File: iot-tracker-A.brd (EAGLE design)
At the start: 21.6 x 19.6 mm, 27 parts, among them IC1 PCF85263ATL_AX, U1 ESP-WROOM-02, U2 TPL5111DDCR, U3 TPS61021ADSGR, Y1 FC-135_32.7680KA-AG3

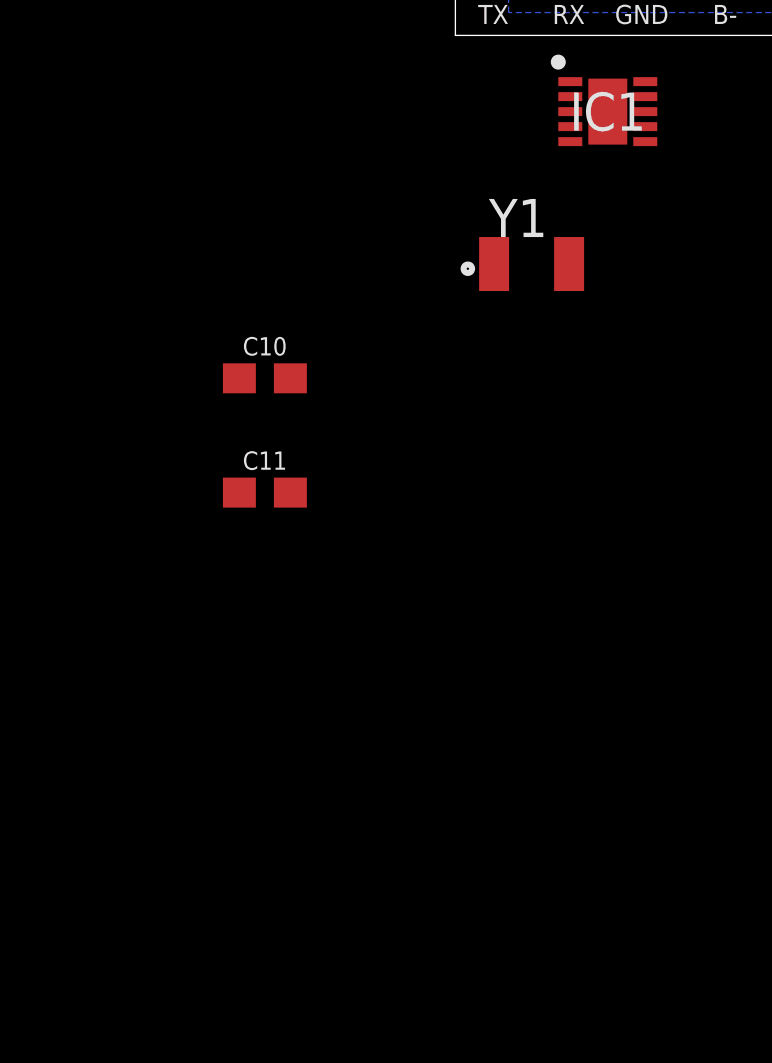
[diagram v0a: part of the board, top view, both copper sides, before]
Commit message: Changed crystal device and added the PNP for DRVN
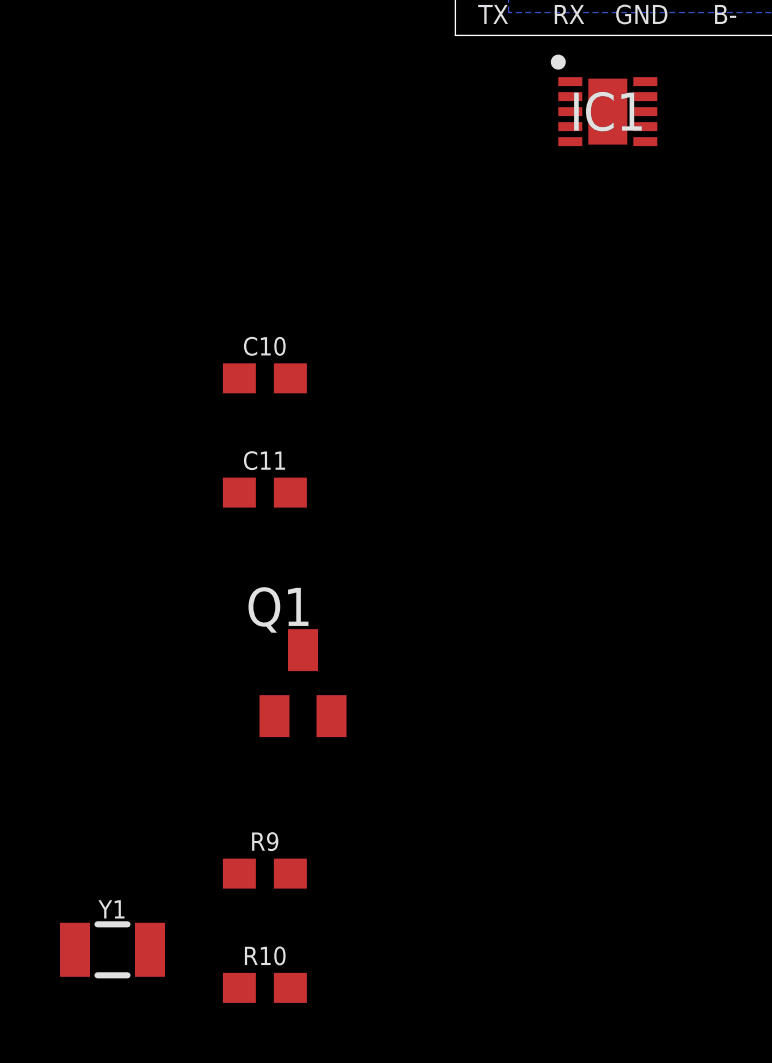
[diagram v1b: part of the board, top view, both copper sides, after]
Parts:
- added Q1: MMBT3906, transistor-pnp:SOT23-BEC
- added R10, R9: 100k, SparkFun-Resistors:0603
- Y1: value FC-135_32.7680KA-AG3 -> 32.768kHz; device IOT-Tracker-A:FC-135_1 -> SparkFun-Clocks:CRYSTAL-SMD-3.2X1.5MM
- moved Y1 26.8 mm to (-11.4, -30.5)
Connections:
- removed net OSCI: IC1.1, Y1.1
- new net N$1: IC1.9, R9.1
- new net N$2: Q1.B, R9.2
- new net N$3: IC1.1, Y1.P$2
- net DRVN: now also Q1.C, R10.2
- net GND: now also R10.1
- net OSCO: now also Y1.P$1; no longer Y1.2
- net V_BATT: now also Q1.E
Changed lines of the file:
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@@
 <attribute name="VALUE" x="5.08" y="-2.54" size="1.27" layer="27" align="center"/>
-</element>
-<element name="Y1" library="IOT-Tracker-A" package="FC-135_1" value="FC-135_32.7680KA-AG3" x="2.54" y="-7.62" smashed="yes">
-<attribute name="DESCRIPTION" value="Crystals 32.768KHz 20ppm 7.0pF -40C +85C" x="2.54" y="-7.62" size="1.778" layer="27" display="off"/>
-<attribute name="HEIGHT" value="mm" x="2.54" y="-7.62" size="1.778" layer="27" display="off"/>
-<attribute name="MANUFACTURER_NAME" value="Epson Timing" x="2.54" y="-7.62" size="1.778" layer="27" display="off"/>
-<attribute name="MANUFACTURER_PART_NUMBER" value="FC-135 32.7680KA-AG3" x="2.54" y="-7.62" size="1.778" layer="27" display="off"/>
-<attribute name="MOUSER_PART_NUMBER" value="732-FC135-32.76KAAG3" x="2.54" y="-7.62" size="1.778" layer="27" display="off"/>
-<attribute name="MOUSER_PRICE-STOCK" value="https://www.mouser.com/Search/Refine.aspx?Keyword=732-FC135-32.76KAAG3" x="2.54" y="-7.62" size="1.778" layer="27" display="off"/>
-<attribute name="NAME" x="2.09671875" y="-6.086340625" size="1.27" layer="25" align="center"/>
-<attribute name="VALUE" x="2.09671875" y="-6.086340625" size="1.27" layer="27" align="center"/>
 </element>
 <element name="C10" library="SparkFun-Capacitors" package="0603" value="0.1uF" x="-6.35" y="-11.43" smashed="yes">
@@
 <attribute name="PROD_ID" value="CAP-00810" x="-6.35" y="-15.24" size="1.778" layer="27" display="off"/>
 <attribute name="VALUE" x="-6.35" y="-16.002" size="0.6096" layer="27" font="vector" ratio="20" align="top-center"/>
+</element>
+<element name="Q1" library="transistor-pnp" library_urn="urn:adsk.eagle:library:399" package="SOT23-BEC" package3d_urn="urn:adsk.eagle:package:28748/2" value="MMBT3906" x="-5.08" y="-21.59" smashed="yes">
+<attribute name="NAME" x="-6.985" y="-19.685" size="1.27" layer="25"/>
+<attribute name="VALUE" x="-6.985" y="-24.765" size="1.27" layer="27"/>
+</element>
+<element name="R9" library="SparkFun-Resistors" package="0603" value="100k" x="-6.35" y="-27.94" smashed="yes">
+<attribute name="NAME" x="-6.35" y="-27.178" size="0.6096" layer="25" font="vector" ratio="20" align="bottom-center"/>
+<attribute name="PROD_ID" value="RES-07828" x="-6.35" y="-27.94" size="1.778" layer="27" display="off"/>
+<attribute name="VALUE" x="-6.35" y="-28.702" size="0.6096" layer="27" font="vector" ratio="20" align="top-center"/>
+</element>
+<element name="R10" library="SparkFun-Resistors" package="0603" value="100k" x="-6.35" y="-31.75" smashed="yes">
+<attribute name="NAME" x="-6.35" y="-30.988" size="0.6096" layer="25" font="vector" ratio="20" align="bottom-center"/>
+<attribute name="PROD_ID" value="RES-07828" x="-6.35" y="-31.75" size="1.778" layer="27" display="off"/>
+<attribute name="VALUE" x="-6.35" y="-32.512" size="0.6096" layer="27" font="vector" ratio="20" align="top-center"/>
+</element>
+<element name="Y1" library="SparkFun-Clocks" package="CRYSTAL-SMD-3.2X1.5MM" value="32.768kHz" x="-11.43" y="-30.48" smashed="yes">
+<attribute name="NAME" x="-11.43" y="-29.437" size="0.6096" layer="25" font="vector" ratio="20" align="bottom-center"/>
+<attribute name="PROD_ID" value="XTAL-13062" x="-11.43" y="-30.48" size="1.778" layer="27" display="off"/>
+<attribute name="VALUE" x="-11.43" y="-31.523" size="0.6096" layer="27" font="vector" ratio="20" align="top-center"/>
 </element>
 </elements>
@@
 <contactref element="C10" pad="1"/>
 <contactref element="C11" pad="1"/>
+<contactref element="R10" pad="1"/>
+<wire x1="-7.2" y1="-15.24" x2="-7.2" y2="-31.75" width="0" layer="19" extent="1-1"/>
+<wire x1="-7.2" y1="-11.43" x2="-7.2" y2="-15.24" width="0" layer="19" extent="1-1"/>
+<wire x1="3.83" y1="-3.54" x2="-7.2" y2="-11.43" width="0" layer="19" extent="1-1"/>
+<wire x1="6.985" y1="3.048" x2="3.83" y2="-3.54" width="0" layer="19" extent="1-1"/>
+<wire x1="9.525" y1="3.048" x2="6.985" y2="3.048" width="0" layer="19" extent="1-1"/>
+<wire x1="13.55" y1="6.731" x2="9.525" y2="3.048" width="0" layer="19" extent="1-1"/>
+<wire x1="13.75" y1="8.267" x2="13.55" y2="6.731" width="0" layer="19" extent="1-1"/>
+<wire x1="12.7" y1="9.017" x2="13.75" y2="8.267" width="0" layer="19" extent="1-1"/>
+<wire x1="12.739" y1="11.557" x2="12.7" y2="9.017" width="0" layer="19" extent="1-1"/>
+<wire x1="12.739" y1="13.081" x2="12.739" y2="11.557" width="0" layer="19" extent="1-1"/>
+<wire x1="9.795" y1="11.581" x2="12.739" y2="11.557" width="0" layer="19" extent="1-1"/>
+<wire x1="16.129" y1="14.771" x2="12.739" y2="13.081" width="0" layer="19" extent="1-1"/>
+<wire x1="17.653" y1="14.771" x2="16.129" y2="14.771" width="0" layer="19" extent="1-1"/>
+<wire x1="20.066" y1="11.977" x2="17.653" y2="14.771" width="0" layer="19" extent="1-1"/>
 <wire x1="20.066" y1="10.375" x2="20.066" y2="11.977" width="0" layer="19" extent="1-1"/>
 <wire x1="18.288" y1="9.105" x2="20.066" y2="10.375" width="0" layer="19" extent="1-1"/>
 <wire x1="19.6875" y1="5.981" x2="18.288" y2="9.105" width="0" layer="19" extent="1-16"/>
-<wire x1="17.653" y1="14.771" x2="20.066" y2="11.977" width="0" layer="19" extent="1-1"/>
-<wire x1="16.129" y1="14.771" x2="17.653" y2="14.771" width="0" layer="19" extent="1-1"/>
-<wire x1="12.739" y1="13.081" x2="16.129" y2="14.771" width="0" layer="19" extent="1-1"/>
-<wire x1="12.739" y1="11.557" x2="12.739" y2="13.081" width="0" layer="19" extent="1-1"/>
-<wire x1="12.7" y1="9.017" x2="12.739" y2="11.557" width="0" layer="19" extent="1-1"/>
-<wire x1="13.75" y1="8.267" x2="12.7" y2="9.017" width="0" layer="19" extent="1-1"/>
-<wire x1="13.55" y1="6.731" x2="13.75" y2="8.267" width="0" layer="19" extent="1-1"/>
-<wire x1="9.795" y1="11.581" x2="12.739" y2="11.557" width="0" layer="19" extent="1-1"/>
 <wire x1="8.068" y1="16.002" x2="9.795" y2="11.581" width="0" layer="19" extent="1-1"/>
 <wire x1="5.207" y1="13.55" x2="8.068" y2="16.002" width="0" layer="19" extent="1-1"/>
@@
 <wire x1="1.905" y1="8.548" x2="1.9025" y2="10.481" width="0" layer="19" extent="1-16"/>
 <wire x1="4.318" y1="8.851" x2="1.905" y2="8.548" width="0" layer="19" extent="1-1"/>
-<wire x1="9.525" y1="3.048" x2="13.55" y2="6.731" width="0" layer="19" extent="1-1"/>
-<wire x1="6.985" y1="3.048" x2="9.525" y2="3.048" width="0" layer="19" extent="1-1"/>
-<wire x1="3.83" y1="-3.54" x2="6.985" y2="3.048" width="0" layer="19" extent="1-1"/>
-<wire x1="-7.2" y1="-11.43" x2="3.83" y2="-3.54" width="0" layer="19" extent="1-1"/>
-<wire x1="-7.2" y1="-15.24" x2="-7.2" y2="-11.43" width="0" layer="19" extent="1-1"/>
 </signal>
 <signal name="DONE" class="2">
@@
 <contactref element="U2" pad="5"/>
 <contactref element="U3" pad="5"/>
-<wire x1="2.667" y1="11.958" x2="11.65" y2="9.767" width="0" layer="19" extent="1-1"/>
+<contactref element="Q1" pad="C"/>
+<contactref element="R10" pad="2"/>
+<wire x1="-5.08" y1="-20.49" x2="-5.5" y2="-31.75" width="0" layer="19" extent="1-1"/>
+<wire x1="2.667" y1="11.958" x2="-5.08" y2="-20.49" width="0" layer="19" extent="1-1"/>
+<wire x1="11.65" y1="9.767" x2="2.667" y2="11.958" width="0" layer="19" extent="1-1"/>
 </signal>
 <signal name="3.3V" class="1">
@@
 <contactref element="C9" pad="2"/>
 <contactref element="C3" pad="1"/>
+<contactref element="C11" pad="2"/>
 <contactref element="IC1" pad="10"/>
-<contactref element="C11" pad="2"/>
 <wire x1="20.066" y1="17.106" x2="19.6875" y2="17.981" width="0" layer="19" extent="1-16"/>
 <wire x1="17.653" y1="16.471" x2="20.066" y2="17.106" width="0" layer="19" extent="1-1"/>
@@
 <contactref element="IC1" pad="3"/>
 <contactref element="C10" pad="2"/>
-<wire x1="11.85" y1="6.731" x2="11.65" y2="8.267" width="0" layer="19" extent="1-1"/>
+<contactref element="Q1" pad="E"/>
+<wire x1="-5.5" y1="-11.43" x2="-4.13" y2="-22.69" width="0" layer="19" extent="1-1"/>
+<wire x1="3.83" y1="-2.54" x2="-5.5" y2="-11.43" width="0" layer="19" extent="1-1"/>
+<wire x1="12.065" y1="3.048" x2="3.83" y2="-2.54" width="0" layer="19" extent="1-1"/>
+<wire x1="11.85" y1="6.731" x2="12.065" y2="3.048" width="0" layer="19" extent="1-1"/>
+<wire x1="11.65" y1="8.267" x2="11.85" y2="6.731" width="0" layer="19" extent="1-1"/>
 <wire x1="9.652" y1="6.266" x2="11.85" y2="6.731" width="0" layer="19" extent="1-1"/>
-<wire x1="12.065" y1="3.048" x2="11.85" y2="6.731" width="0" layer="19" extent="1-1"/>
 <wire x1="5.207" y1="11.85" x2="9.652" y2="6.266" width="0" layer="19" extent="1-1"/>
 <wire x1="3.617" y1="11.958" x2="5.207" y2="11.85" width="0" layer="19" extent="1-1"/>
 <wire x1="3.617" y1="14.458" x2="3.617" y2="11.958" width="0" layer="19" extent="1-1"/>
-<wire x1="3.83" y1="-2.54" x2="12.065" y2="3.048" width="0" layer="19" extent="1-1"/>
-<wire x1="-5.5" y1="-11.43" x2="3.83" y2="-2.54" width="0" layer="19" extent="1-1"/>
 </signal>
 <signal name="IO4_LED">
@@
 <wire x1="9.652" y1="8.466" x2="11.65" y2="8.767" width="0" layer="19" extent="1-1"/>
 </signal>
-<signal name="OSCI">
-<contactref element="Y1" pad="1"/>
+<signal name="OSCO">
+<contactref element="IC1" pad="2"/>
+<contactref element="Y1" pad="P$1"/>
+<wire x1="3.83" y1="-2.04" x2="-12.68" y2="-30.48" width="0" layer="19" extent="1-1"/>
+</signal>
+<signal name="N$1">
+<contactref element="R9" pad="1"/>
+<contactref element="IC1" pad="9"/>
+<wire x1="6.33" y1="-2.04" x2="-7.2" y2="-27.94" width="0" layer="19" extent="1-1"/>
+</signal>
+<signal name="N$2">
+<contactref element="R9" pad="2"/>
+<contactref element="Q1" pad="B"/>
+<wire x1="-6.03" y1="-22.69" x2="-5.5" y2="-27.94" width="0" layer="19" extent="1-1"/>
+</signal>
+<signal name="N$3">
 <contactref element="IC1" pad="1"/>
-<wire x1="3.83" y1="-1.54" x2="1.29" y2="-7.62" width="0" layer="19" extent="1-1"/>
-</signal>
-<signal name="OSCO">
-<contactref element="Y1" pad="2"/>
-<contactref element="IC1" pad="2"/>
-<wire x1="3.83" y1="-2.04" x2="3.79" y2="-7.62" width="0" layer="19" extent="1-1"/>
+<contactref element="Y1" pad="P$2"/>
+<wire x1="3.83" y1="-1.54" x2="-10.18" y2="-30.48" width="0" layer="19" extent="1-1"/>
 </signal>
 </signals>

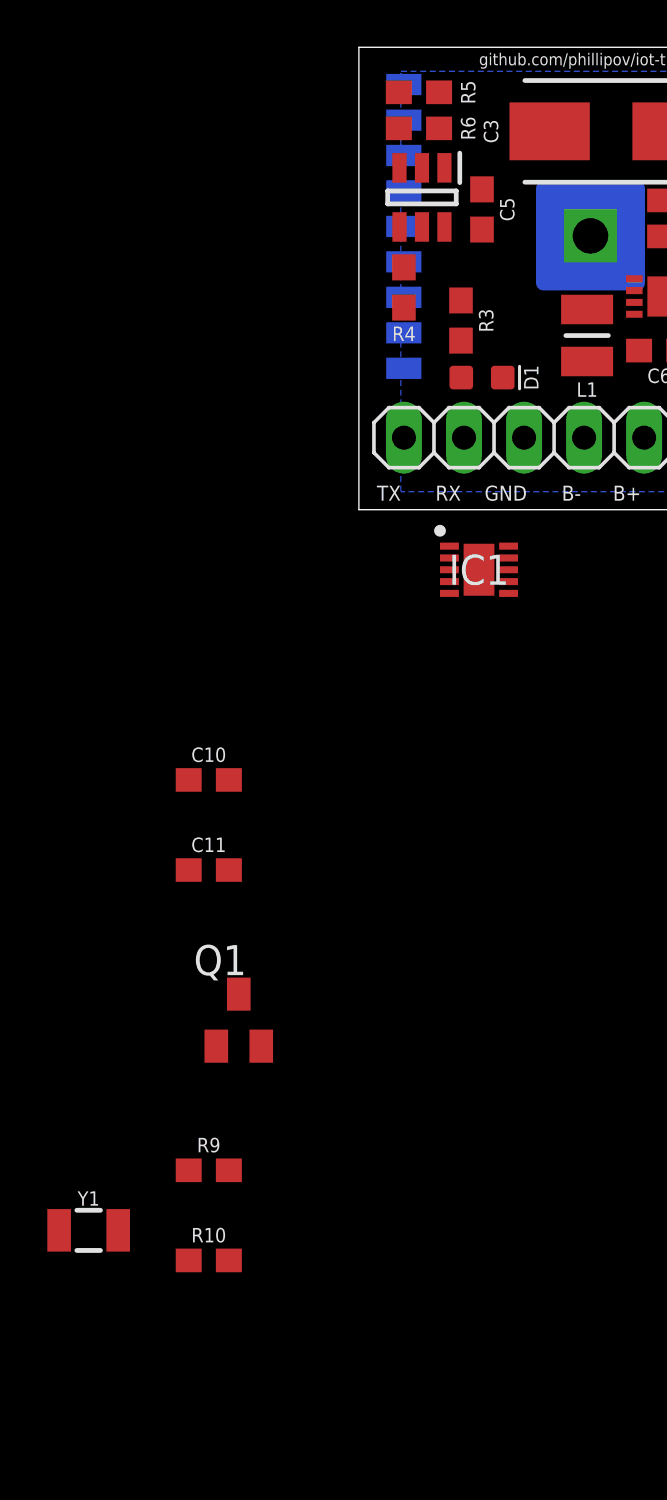
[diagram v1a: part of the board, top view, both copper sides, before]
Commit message: Fully integrated RTC into the schematic
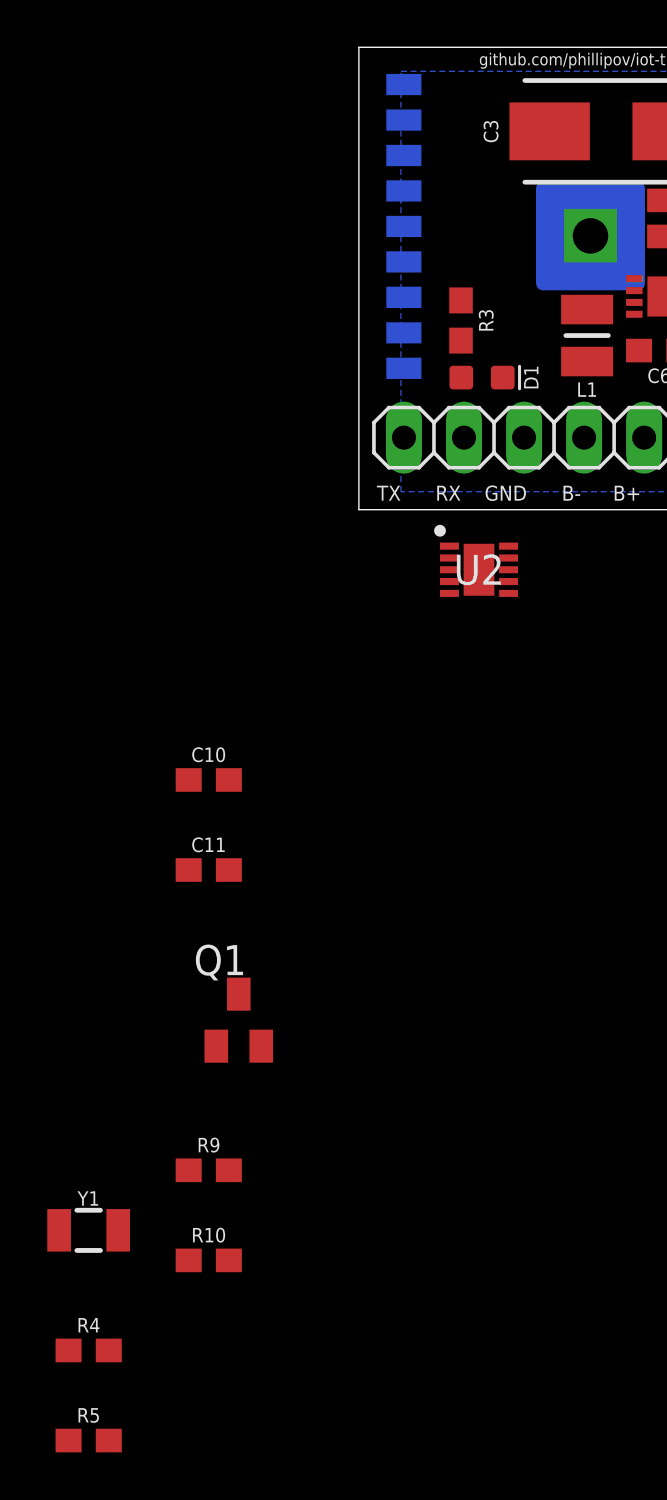
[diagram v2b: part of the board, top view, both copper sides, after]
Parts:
- removed C5: 0.1uF, SparkFun-Capacitors:0603
- removed IC1: PCF85263ATL_AX, IOT-Tracker-A:SON50P260X260X50-11N
- removed R6: 340k, SparkFun-Resistors:0603
- R4: value 10k -> 4.7k
- R5: value 340k -> 4.7k
- U2: value TPL5111DDCR -> PCF85263ATL_AX; device TPL5111DDCR:SOT95P280X110-6N -> IOT-Tracker-A:SON50P260X260X50-11N
- moved R5 58.7 mm to (-11.4, -39.4), turned to 0 degrees
- moved R4 46.9 mm to (-11.4, -35.6), turned to 0 degrees
- moved U2 15.9 mm to (5.08, -2.54), turned to 0 degrees
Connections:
- removed net DELAY: R5.2, R6.2, U2.3
- removed net DONE: R4.1, U1.14, U2.4
- removed net IO4_LED: D1.A, U1.10
- removed net LED_GND: D1.C, R3.2
- new net IO12_LED: D1.A, U1.4
- new net LED_CATH: D1.C, R3.1
- new net SCL: R4.1, U1.10, U2.7
- new net SDA: R5.1, U1.14, U2.6
- net 3.3V: now also R4.2, R5.2, U2.10; no longer IC1.10
- net DRVN: no longer U2.5
- net GND: now also R3.2, U2.5; no longer C5.1, IC1.5, R3.1, R4.2, R5.1, R6.1, U2.2
- net N$1: now also U2.9; no longer IC1.9
- net N$3: now also U2.1; no longer IC1.1
- net OSCO: now also U2.2; no longer IC1.2
- net V_BATT: now also U2.3; no longer C5.2, IC1.3, U2.1, U2.6

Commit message: Minor component changes and net renaming
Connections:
- net N$1 renamed INTA
- net N$2 renamed INTA_PNP_B
- net N$3 renamed OSCI
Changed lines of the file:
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@@
 </elements>
 <signals>
-<signal name="GND" class="1">
+<signal name="GND" class="1" airwireshidden="yes">
 <contactref element="C4" pad="1"/>
 <contactref element="R2" pad="2"/>
@@
 <wire x1="11.65" y1="9.767" x2="-5.08" y2="-20.49" width="0" layer="19" extent="1-1"/>
 </signal>
-<signal name="3.3V" class="1">
+<signal name="3.3V" class="1" airwireshidden="yes">
 <contactref element="U1" pad="1"/>
 <contactref element="R1" pad="1"/>
@@
 <wire x1="3.83" y1="-2.04" x2="-12.68" y2="-30.48" width="0" layer="19" extent="1-1"/>
 </signal>
-<signal name="N$1">
+<signal name="INTA">
 <contactref element="R9" pad="1"/>
 <contactref element="U2" pad="9"/>
 <wire x1="6.33" y1="-2.04" x2="-7.2" y2="-27.94" width="0" layer="19" extent="1-1"/>
 </signal>
-<signal name="N$3">
+<signal name="OSCI">
 <contactref element="U2" pad="1"/>
 <contactref element="Y1" pad="P$2"/>
@@
 <wire x1="1.9025" y1="11.981" x2="6.33" y2="-3.54" width="0" layer="19" extent="1-16"/>
 </signal>
-<signal name="N$2">
+<signal name="INTA_PNP_B">
 <contactref element="R9" pad="2"/>
 <contactref element="Q1" pad="B"/>
